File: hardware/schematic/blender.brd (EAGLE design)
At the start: 122 x 44 mm, 102 parts, among them IC1 MEGA32-A, IC2 AD7793, Q1 IRF540, Q10 IRF540, Q2 IRF540, Q5 BS170, Q6 BS170, Q7 BS170, Q8 BS170, Q9 BS170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

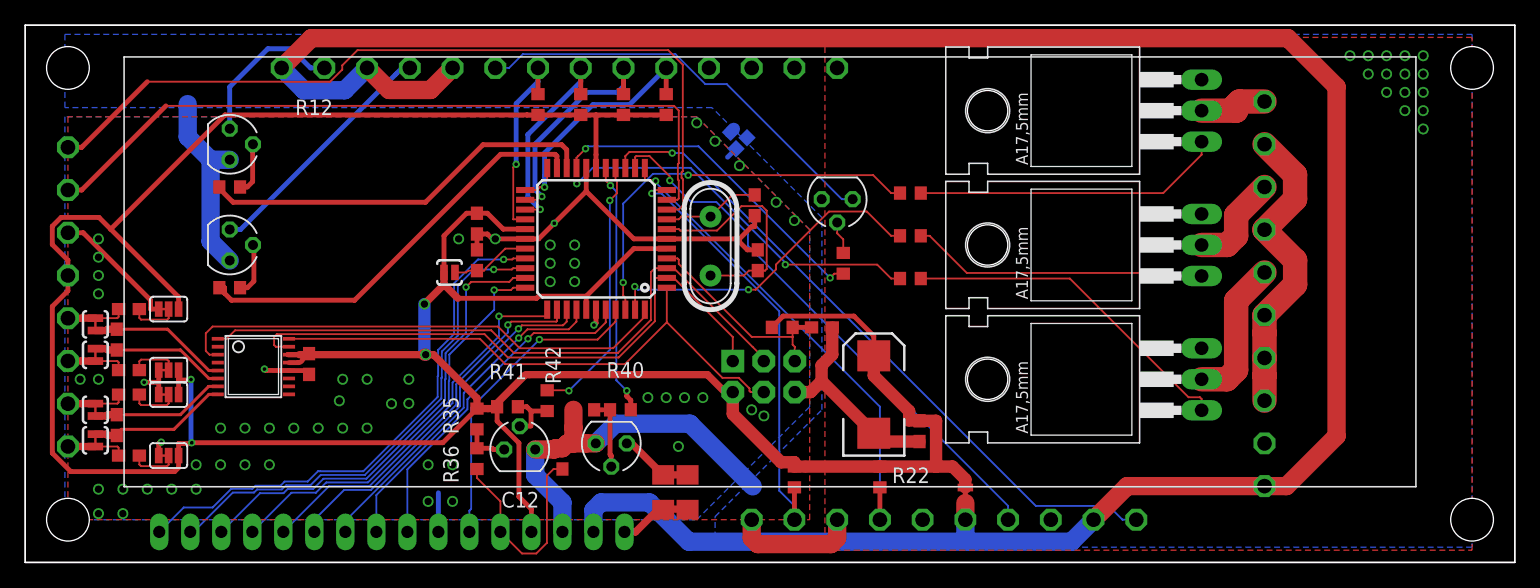
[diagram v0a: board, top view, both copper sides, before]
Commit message: some tweaks for schematic (board destroyed), added TODOs for sch (inside sch)
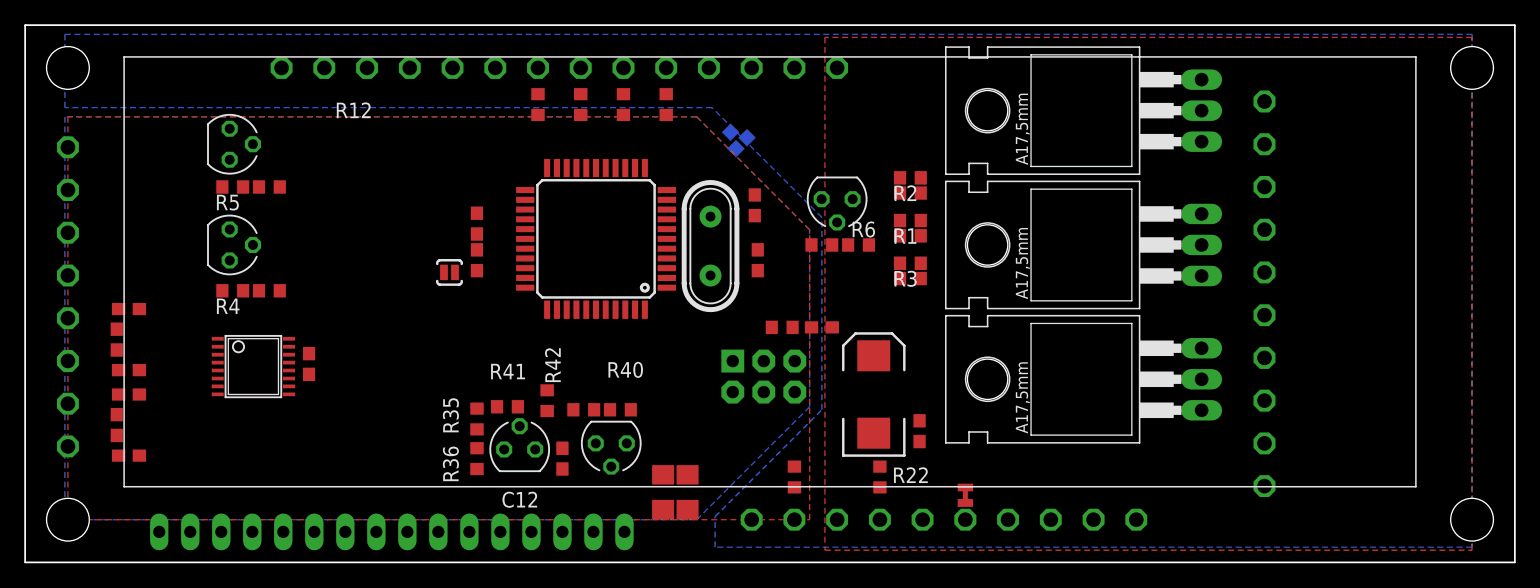
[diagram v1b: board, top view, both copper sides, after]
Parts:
- removed SJ1, SJ15, SJ16, SJ2: JUMPER-PAD-3-2OF3_NC_BY_TRACE_SMALL, SparkFun-Passives:PAD-JUMPER-3-2OF3_NC_BY_TRACE_YES_SILK_FULL_BOX
- removed SJ13, SJ14, SJ7, SJ8: JUMPER-PAD-2-NC_BY_TRACE, SparkFun-Passives:PAD-JUMPER-2-NC_BY_TRACE_YES_SILK
- added R1, R2, R3, R4, R5, R6: 10k, resistor:R0603
- C10, C6, C7, C9: value DNP -> 10nF
- C11, C8: value DNP -> 100nF
- moved R12 3.26 mm to (20.0, 22.2)
- moved R16 3.25 mm to (20.0, 30.8), turned to 180 degrees
- moved R14 2.30 mm to (65.2, 26.0), turned to 0 degrees
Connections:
- removed net N$1: C9.2, SJ15.2
- removed net N$2: C10.1, SJ16.2
- removed net N$3: C6.2, SJ1.2
- removed net N$56: C11.1, IC2.5, SJ14.2
- removed net N$57: C8.2, IC2.7, SJ7.2
- removed net N$58: C8.1, IC2.8, SJ13.2
- removed net N$62: C10.2, O2_1_IN-.P$1, SJ8.1
- removed net N$9: C7.1, SJ2.2
- net AGND: now also C10.1, C6.2, C7.1, C9.2; no longer SJ1.3, SJ15.3, SJ16.3, SJ2.3
- net GND: now also R1.2, R2.2, R3.2, R4.2, R5.2, R6.2
- net N$27: now also R1.1
- net N$28: now also R2.1
- net N$29: now also R3.1
- net N$31: now also R6.1
- net N$32: now also R4.1
- net N$33: now also R5.1
- net N$55: now also C10.2, O2_1_IN-.P$1; no longer SJ8.2
- net N$59: now also C8.2, IC2.7; no longer SJ7.1
- net N$60: now also C8.1, IC2.8; no longer SJ13.1
- net N$64: now also C11.1, IC2.5; no longer SJ14.1
- net VDD: no longer SJ1.1, SJ15.1, SJ16.1, SJ2.1
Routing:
- net VDD: track 279.7 -> 0.00 mm, vias 4 -> 0
- net +5V: track 205.7 -> 0.00 mm
- net AGND: track 74.9 -> 0.00 mm, vias 59 -> 0
- net N$45: track 67.4 -> 0.00 mm
- net N$46: track 61.3 -> 0.00 mm
- net GND: track 57.8 -> 0.00 mm, vias 15 -> 0
- net N$47: track 55.4 -> 0.00 mm, vias 1 -> 0
- net N$14: track 54.2 -> 0.00 mm
- net N$13: track 49.2 -> 0.00 mm
- net N$12: track 46.5 -> 0.00 mm
- net N$48: track 45.3 -> 0.00 mm, vias 1 -> 0
- net DB7: track 43.9 -> 0.00 mm, vias 1 -> 0
- net N$15: track 41.1 -> 0.00 mm
- net DB6: track 41.0 -> 0.00 mm, vias 1 -> 0
- net N$40: track 39.9 -> 0.00 mm, vias 1 -> 0
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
